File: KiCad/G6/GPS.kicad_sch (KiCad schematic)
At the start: 6 parts, among them IC1 BGU7004,115, IC2 LD56020M180R, U2 NEO-M9N-00B

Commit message: im sorry parsa :/
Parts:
- L1: footprint LQW15AN5N6G80D:INDC1006X60N -> Inductor_SMD:L_1206_3216Metric
- U12: footprint Library:RSF-1575.420-24000-3030-TR -> CC0603KRXQRQBB104:RSF-1575.420-24000-3030-TR
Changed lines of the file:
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@@
 			)
 		)
-		(property "Footprint" "LQW15AN5N6G80D:INDC1006X60N"
+		(property "Footprint" "Inductor_SMD:L_1206_3216Metric"
 			(at 95.25 105.41 0)
 			(effects
@@
 			)
 		)
-		(property "Footprint" "Library:RSF-1575.420-24000-3030-TR"
+		(property "Footprint" "CC0603KRXQRQBB104:RSF-1575.420-24000-3030-TR"
 			(at 78.74 106.68 0)
 			(effects

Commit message: sasha sneaky academic
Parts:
- added C3: 0.1, symbol Device:C
- renumbered U12 to U4, U2 to U5
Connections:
- net 3.3v: now also U5.22 (V_BCKP), C3.2
- net GNDD: no longer U5.10 (GND)
- net R: no longer names the net of U5.21 (RXD/SPI_MOSI)
- net T: no longer names the net of U5.20 (TXD/SPI_MISO)
- new net GND: C3.1, U5.10 (GND)

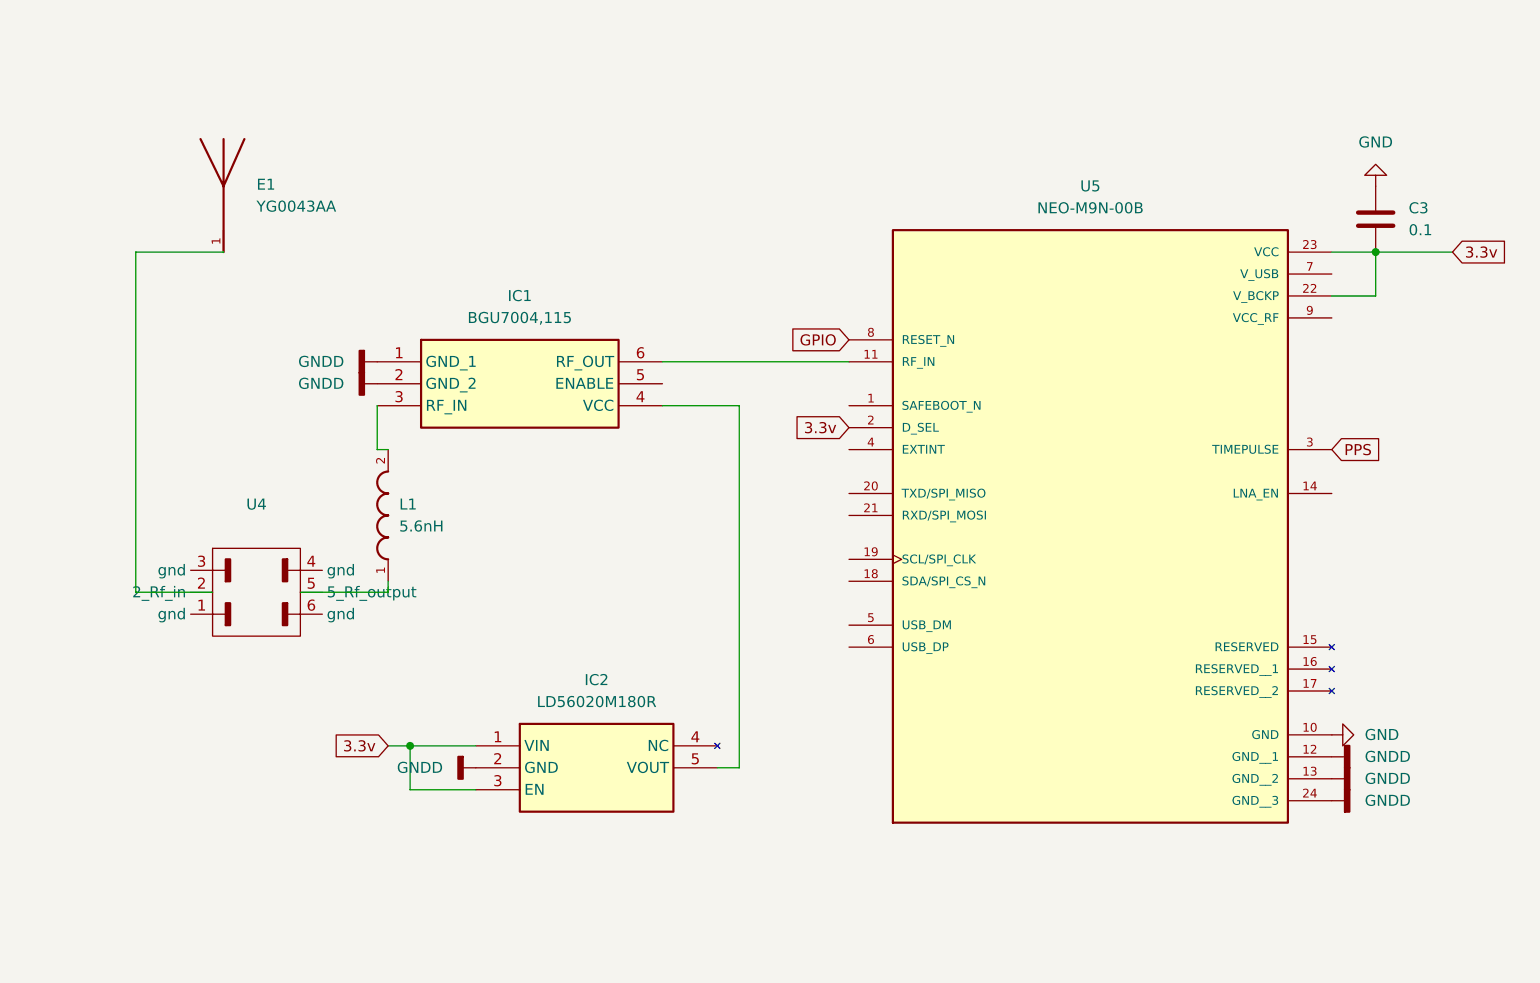
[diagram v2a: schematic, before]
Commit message: errrrrr i cant find a umcx connector they all say there like $50??
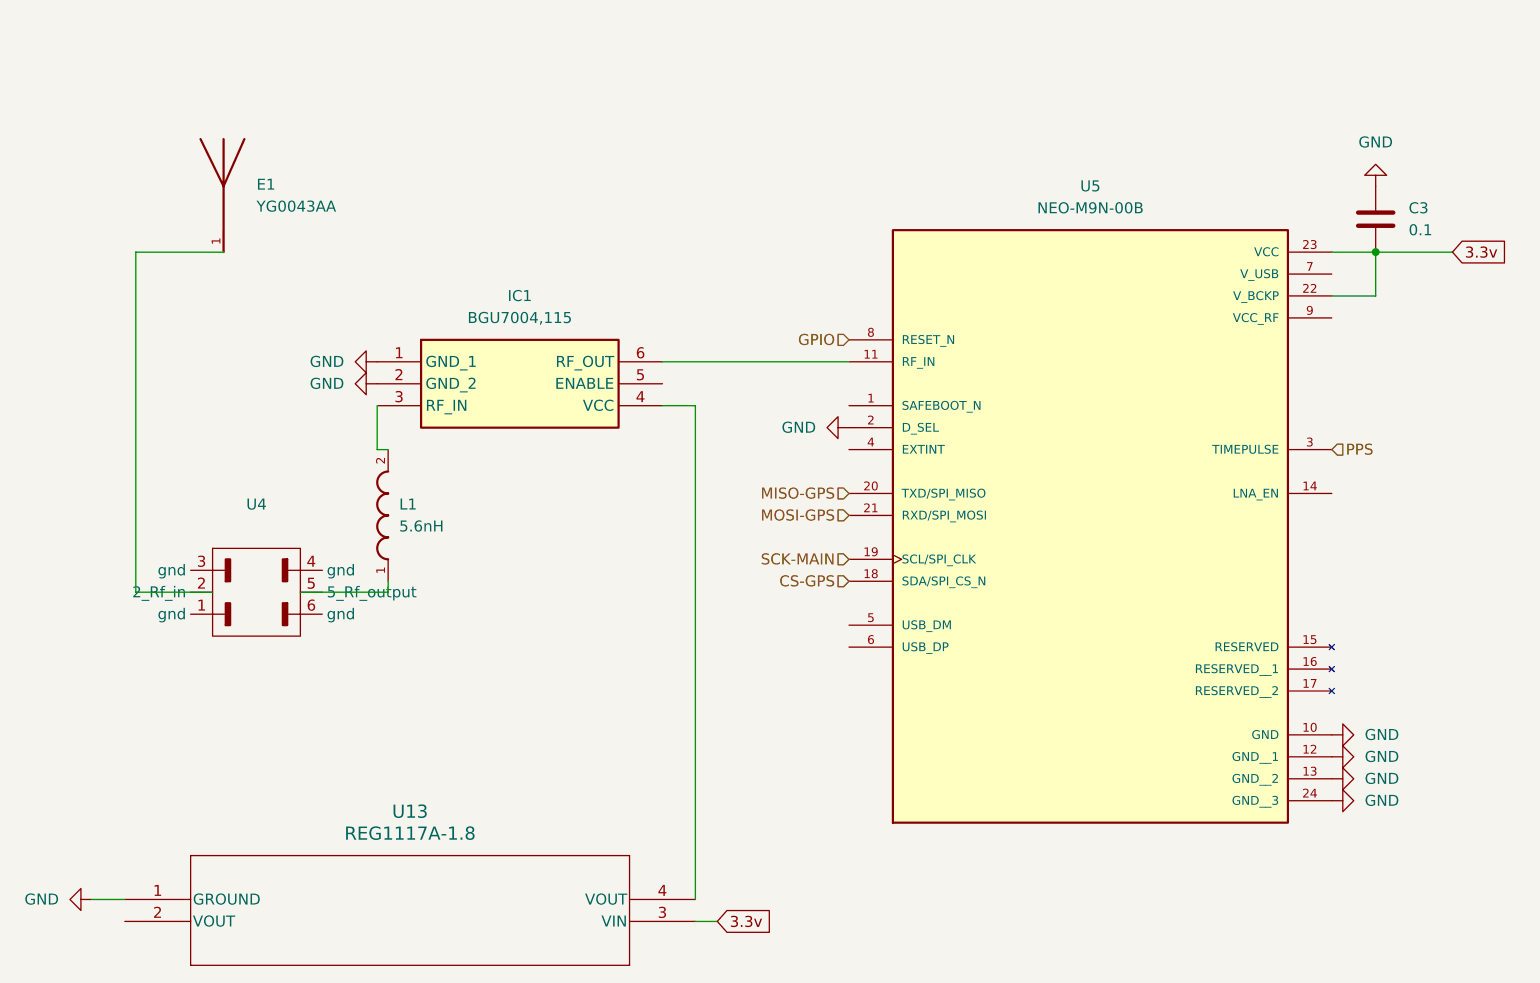
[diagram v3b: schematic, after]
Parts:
- removed IC2: LD56020M180R, Package_TO_SOT_SMD:SOT-23-5, symbol LD56020M180R:LD56020M180R
- added U13: REG1117A-1.8, CC0603KRXQRQBB104:LDO1.8, symbol REG1117A:REG1117A-1.8
- C3: footprint (none) -> CC0603KRXQRQBB104:.1CAP_CC1206_YAG
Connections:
- net 3.3v: now also U13.3 (VIN); no longer U5.2 (D_SEL)
- net GND: now also IC1.1 (GND_1), IC1.2 (GND_2), U5.12 (GND__1), U5.13 (GND__2), U5.2 (D_SEL), U5.24 (GND__3), U13.1 (GROUND)
- net GNDD: no longer IC1.1 (GND_1), IC1.2 (GND_2), U5.12 (GND__1), U5.13 (GND__2), U5.24 (GND__3)
- net at IC1.4 (VCC): now also U13.4 (VOUT)
- net CS-GPS: now reaches U5.18 (SDA/SPI_CS_N)
- net SCK-MAIN: now reaches U5.19 (SCL/SPI_CLK)
- net MISO-GPS: now reaches U5.20 (TXD/SPI_MISO)
- net MOSI-GPS: now reaches U5.21 (RXD/SPI_MOSI)

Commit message: g6
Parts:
- removed E1: YG0043AA, YG0043AA:XDCR_YG0043AA, symbol YG0043AA:YG0043AA
- added J2: CONMHF1-SMD-T, CONMHF1_SMD_T:TE_CONMHF1-SMD-T, symbol CONMHF1-SMD-T:CONMHF1-SMD-T
- added R10: 10k, Resistor_SMD:R_0805_2012Metric, symbol Device:R
- added R5: 1k, Resistor_SMD:R_0805_2012Metric, symbol Device:R
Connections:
- net GNDD is gone; now on net GND: U4.1 (gnd), U4.3 (gnd), U4.4 (gnd), U4.6 (gnd)
- net 3.3v: now also R5.2
- net GND: now also J2.2, J2.3, J2.4, R10.2
- net ENABLE: now reaches IC1.5 (ENABLE)
- net ENABLE: now also R10.1, R5.1
- net at U4.2 (Rf_in): now also J2.1
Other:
- moved on the sheet: U4

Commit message: changed the inductor sizing
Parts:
- L1: footprint Inductor_SMD:L_1206_3216Metric -> Inductor_SMD:L_1008_2520Metric
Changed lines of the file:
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@@
 			)
 		)
-		(property "Footprint" "Inductor_SMD:L_1206_3216Metric"
+		(property "Footprint" "Inductor_SMD:L_1008_2520Metric"
 			(at 95.25 105.41 0)
 			(effects
